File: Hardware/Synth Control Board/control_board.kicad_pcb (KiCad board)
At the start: 2 copper layers, 127 x 177.8 mm, 36 parts, among them J1 Conn_01x13, J2 Conn_01x03, J3 Conn_01x13, J4 Conn_01x13, J5 Conn_01x02, J6 Conn_01x13, SW1 SW_DPDT_x2, SW10 SW_SPST, SW11 SW_SPST, SW12 SW_SPST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

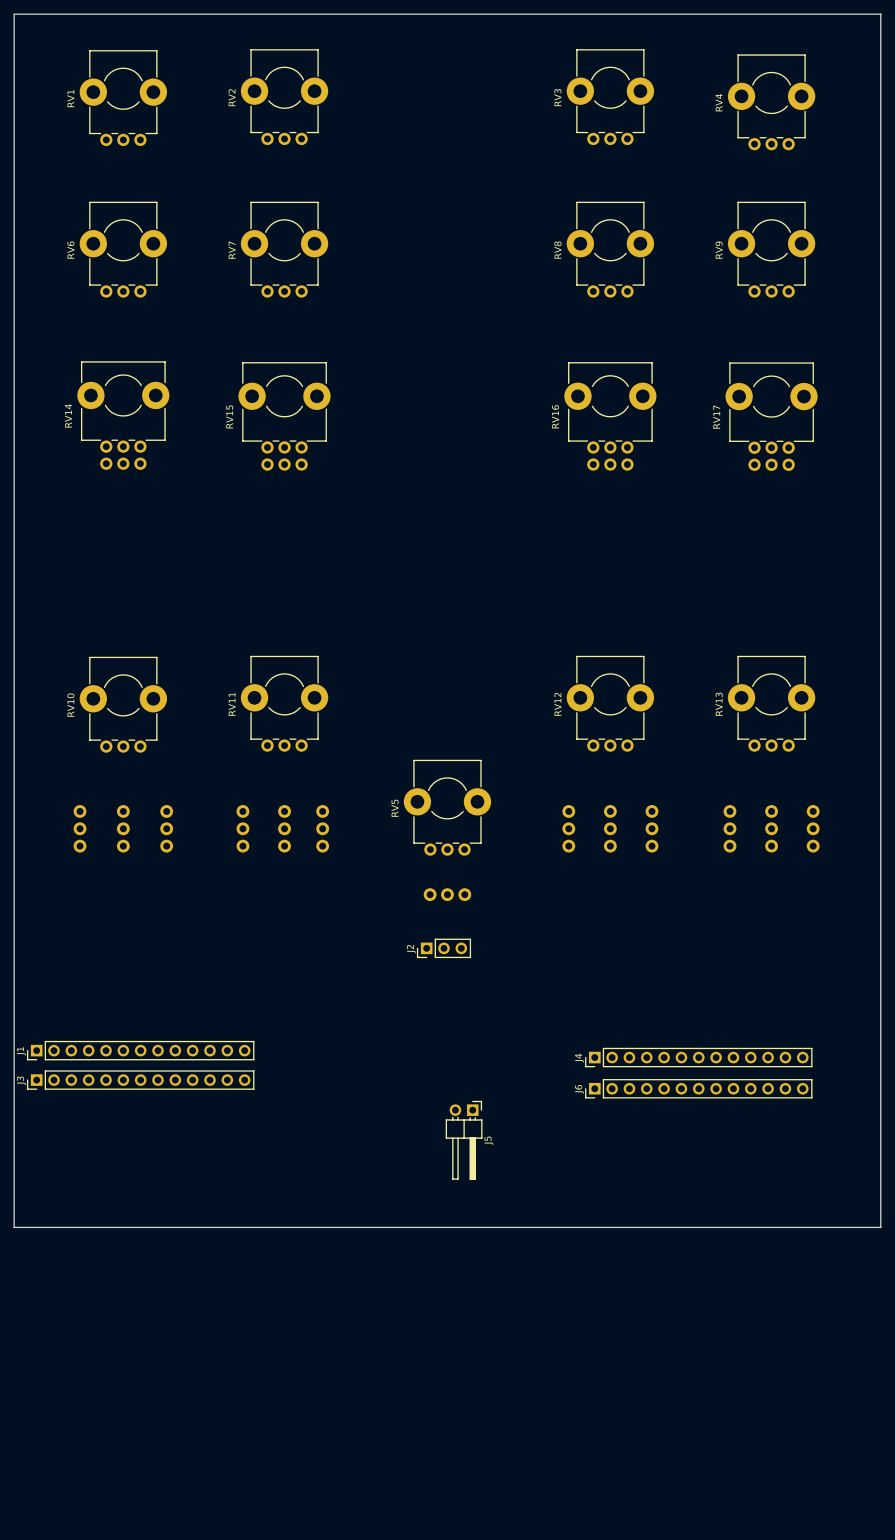
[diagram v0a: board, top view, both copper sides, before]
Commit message: add volume pots to control board
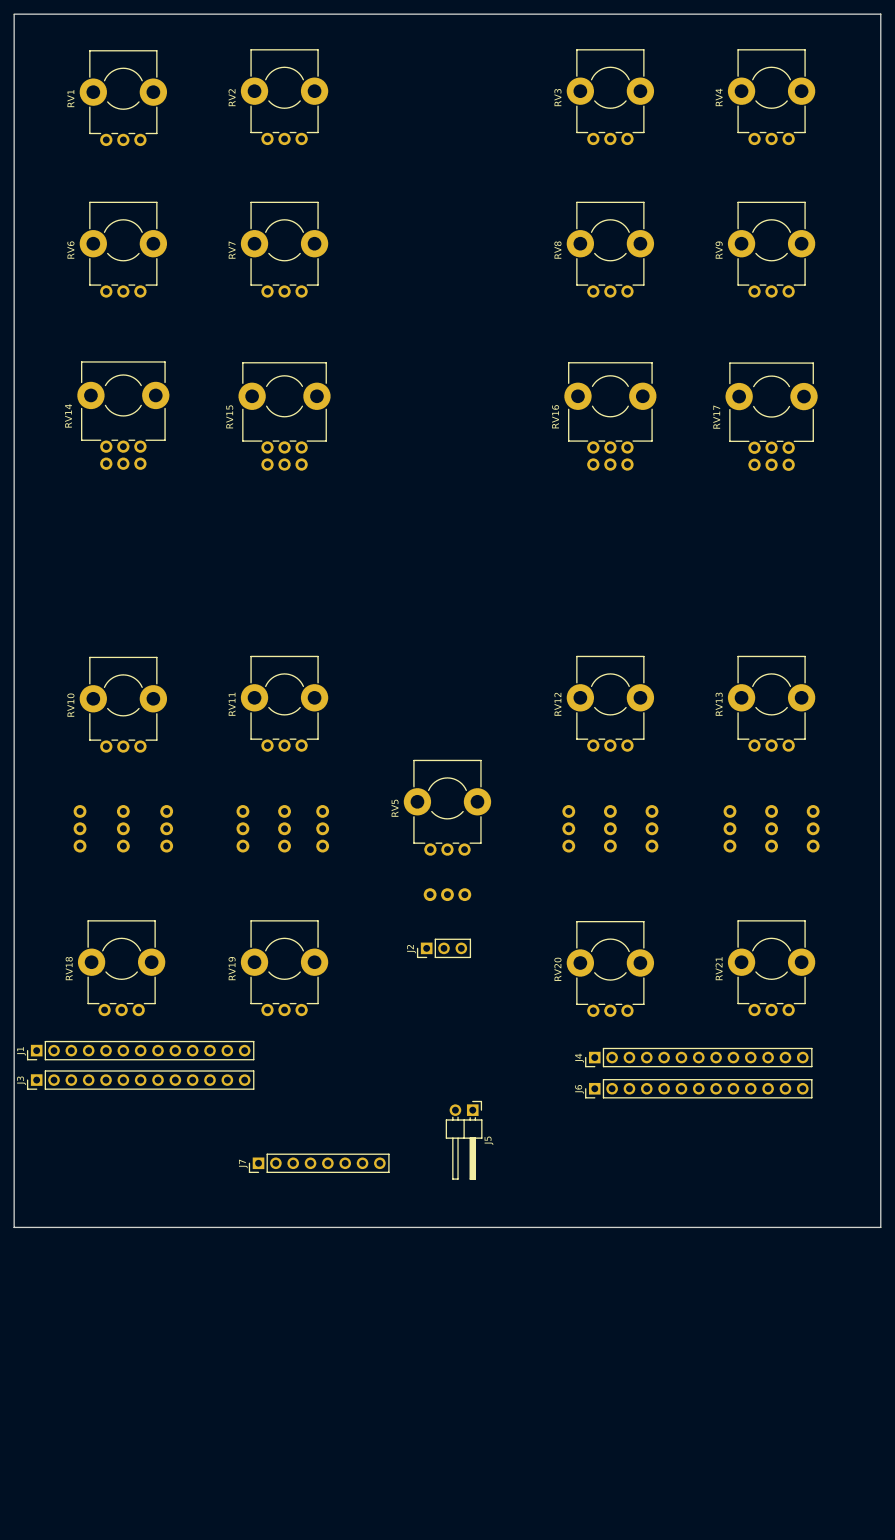
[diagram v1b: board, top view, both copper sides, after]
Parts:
- added J7: Conn_01x08, Pin_Headers:Pin_Header_Straight_1x08_Pitch2.54mm, F.Cu at (35.8, 168.4)
- added RV18: 100kA, Potentiometers:Potentiometer_Bourns_PTV09A-1_Horizontal, F.Cu at (18.2, 145.9)
- added RV19: 100kA, Potentiometers:Potentiometer_Bourns_PTV09A-1_Horizontal, F.Cu at (42.1, 145.9)
- added RV20: 100kA, Potentiometers:Potentiometer_Bourns_PTV09A-1_Horizontal, F.Cu at (89.9, 146.1)
- added RV21: 100kA, Potentiometers:Potentiometer_Bourns_PTV09A-1_Horizontal, F.Cu at (113.5, 145.9)
- moved RV4 0.76 mm to (113.5, 18.3)

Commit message: place MCU footprints
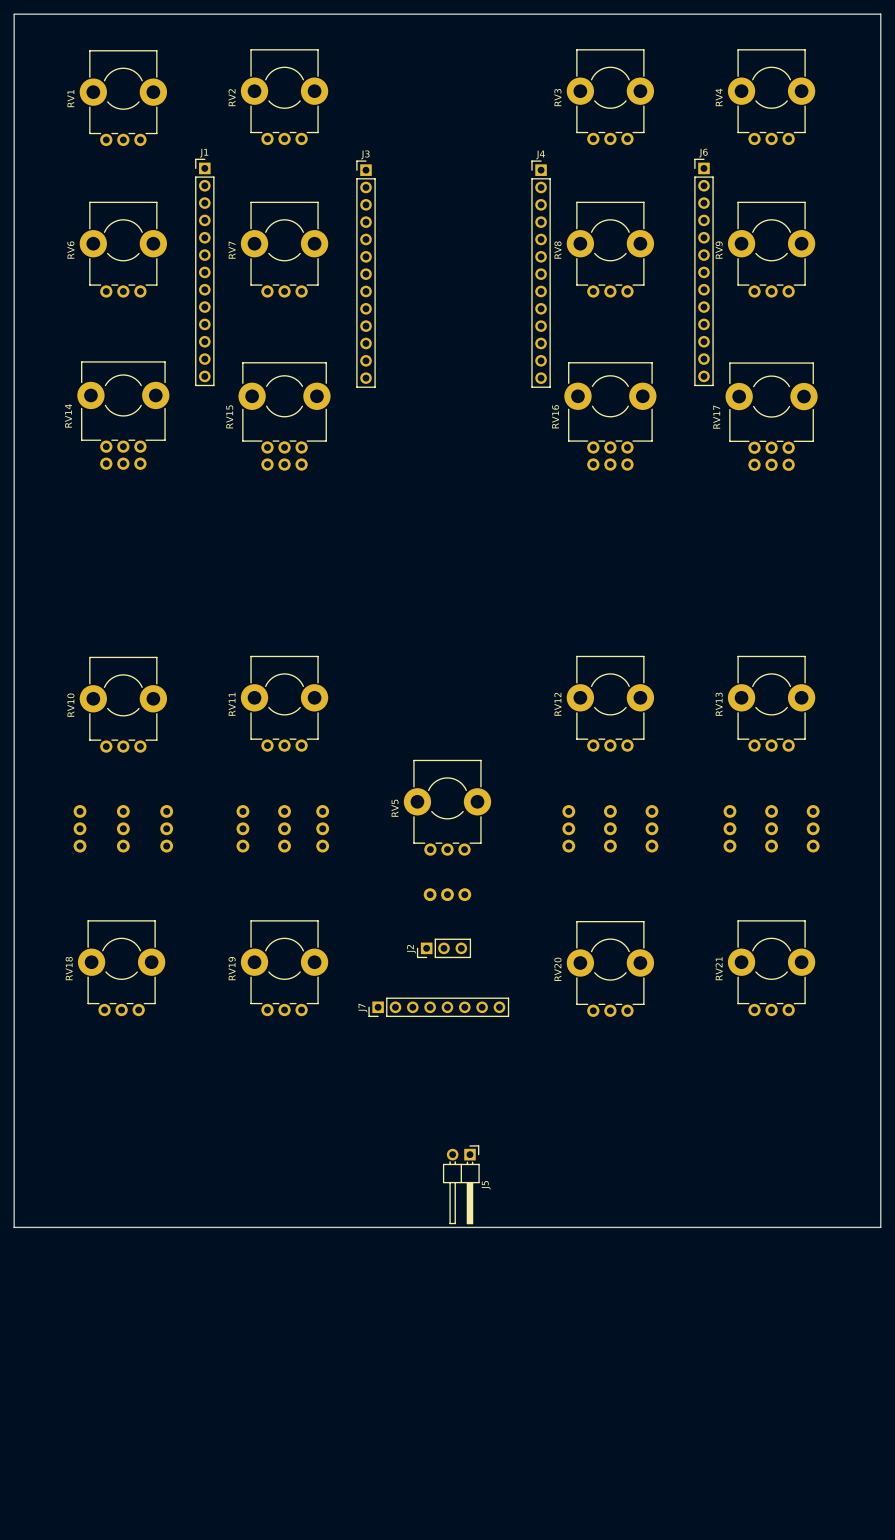
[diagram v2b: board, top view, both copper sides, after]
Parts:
- moved J3 141.8 mm to (51.6, 22.9), turned to 0 degrees
- moved J6 135.8 mm to (101.1, 22.6), turned to 0 degrees
- moved J1 131.6 mm to (27.9, 22.6), turned to 0 degrees
- moved J4 130.3 mm to (77.2, 22.9), turned to 0 degrees
- moved J7 28.8 mm to (53.3, 145.5)
- moved J5 6.53 mm to (66.8, 167.1)

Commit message: add LFO mod pots to control board and fix pot placement
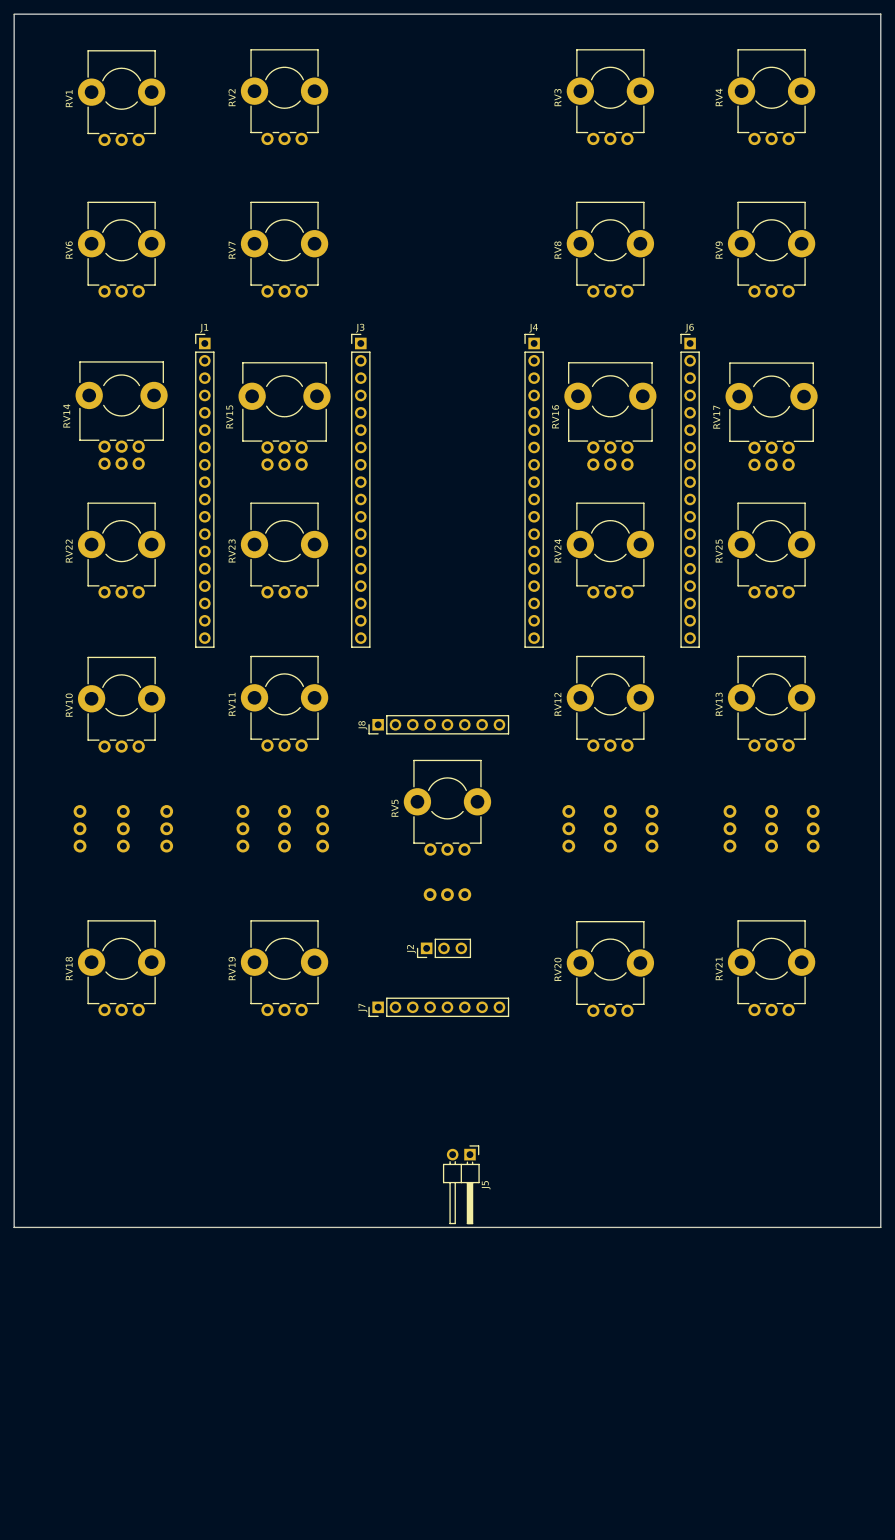
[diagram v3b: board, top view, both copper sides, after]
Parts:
- added J8: Conn_01x08, Pin_Headers:Pin_Header_Straight_1x08_Pitch2.54mm, F.Cu at (53.3, 104.1)
- added RV22: 100kA, Potentiometers:Potentiometer_Bourns_PTV09A-1_Horizontal, F.Cu at (18.2, 84.7)
- added RV23: 100kA, Potentiometers:Potentiometer_Bourns_PTV09A-1_Horizontal, F.Cu at (42.1, 84.7)
- added RV24: 100kA, Potentiometers:Potentiometer_Bourns_PTV09A-1_Horizontal, F.Cu at (89.9, 84.7)
- added RV25: 100kA, Potentiometers:Potentiometer_Bourns_PTV09A-1_Horizontal, F.Cu at (113.5, 84.7)
- J1, J3, J4, J6: value Conn_01x13 -> Conn_01x18; footprint Pin_Headers:Pin_Header_Straight_1x13_Pitch2.54mm -> Pin_Headers:Pin_Header_Straight_1x18_Pitch2.54mm
- moved J6 25.7 mm to (99.1, 48.3)
- moved J1 25.7 mm to (27.9, 48.3)
- moved J4 25.4 mm to (76.2, 48.3)
- moved J3 25.4 mm to (50.8, 48.3)
- moved RV1 0.25 mm to (18.2, 18.4)
- moved RV10 0.25 mm to (18.2, 107.3)
- moved RV14 0.25 mm to (18.2, 63.4)
- moved RV6 0.25 mm to (18.2, 40.6)
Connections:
- J1 pad 10: /osc1_repeat -> /osc1_speed
- J1 pad 11: /osc1_quant -> +5V
- J1 pad 12: GND -> /envelope_pwm_bypass_in_1
- J1 pad 13: GNDD -> /envelope_pwm_bypass_out_1
- J1 pad 4: /osc1_speed -> +5V
- J1 pad 5: /freq_in_1 -> /freq_out_1
- J1 pad 7: /freq_out_1 -> /freq_in_1
- J1 pad 8: /envelope_pwm_bypass_in_1 -> /lfo_in_1
- J1 pad 9: /envelope_pwm_bypass_out_1 -> /lfo_out_1
- J3 pad 10: /osc2_repeat -> /osc2_speed
- J3 pad 11: /osc2_quant -> +5V
- J3 pad 12: GND -> /envelope_pwm_bypass_in_2
- J3 pad 13: GNDD -> /envelope_pwm_bypass_out_2
- J3 pad 4: /osc2_speed -> +5V
- J3 pad 5: /freq_in_2 -> /freq_out_2
- J3 pad 7: /freq_out_2 -> /freq_in_2
- J3 pad 8: /envelope_pwm_bypass_in_2 -> /lfo_in_2
- J3 pad 9: /envelope_pwm_bypass_out_2 -> /lfo_out_2
- J4 pad 10: /osc3_repeat -> /osc3_speed
- J4 pad 11: /osc3_quant -> +5V
- J4 pad 12: GND -> /envelope_pwm_bypass_in_3
- J4 pad 13: GNDD -> /envelope_pwm_bypass_out_3
- J4 pad 4: /osc3_speed -> +5V
- J4 pad 5: /freq_in_3 -> /freq_out_3
- J4 pad 7: /freq_out_3 -> /freq_in_3
- J4 pad 8: /envelope_pwm_bypass_in_3 -> /lfo_in_3
- J4 pad 9: /envelope_pwm_bypass_out_3 -> /lfo_out_3
- J6 pad 10: /osc4_repeat -> /osc4_speed
- J6 pad 11: /osc4_quant -> +5V
- J6 pad 12: GND -> /envelope_pwm_bypass_in_4
- J6 pad 13: GNDD -> /envelope_pwm_bypass_out_4
- J6 pad 4: /osc4_speed -> +5V
- J6 pad 5: /freq_in_4 -> /freq_out_4
- J6 pad 7: /freq_out_4 -> /freq_in_4
- J6 pad 8: /envelope_pwm_bypass_in_4 -> /lfo_in_4
- J6 pad 9: /envelope_pwm_bypass_out_4 -> /lfo_out_4
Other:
- rule trace_min: 0.2 -> 0.0889

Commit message: route traces to bypass caps on MCU. control board and connectors are WIP.
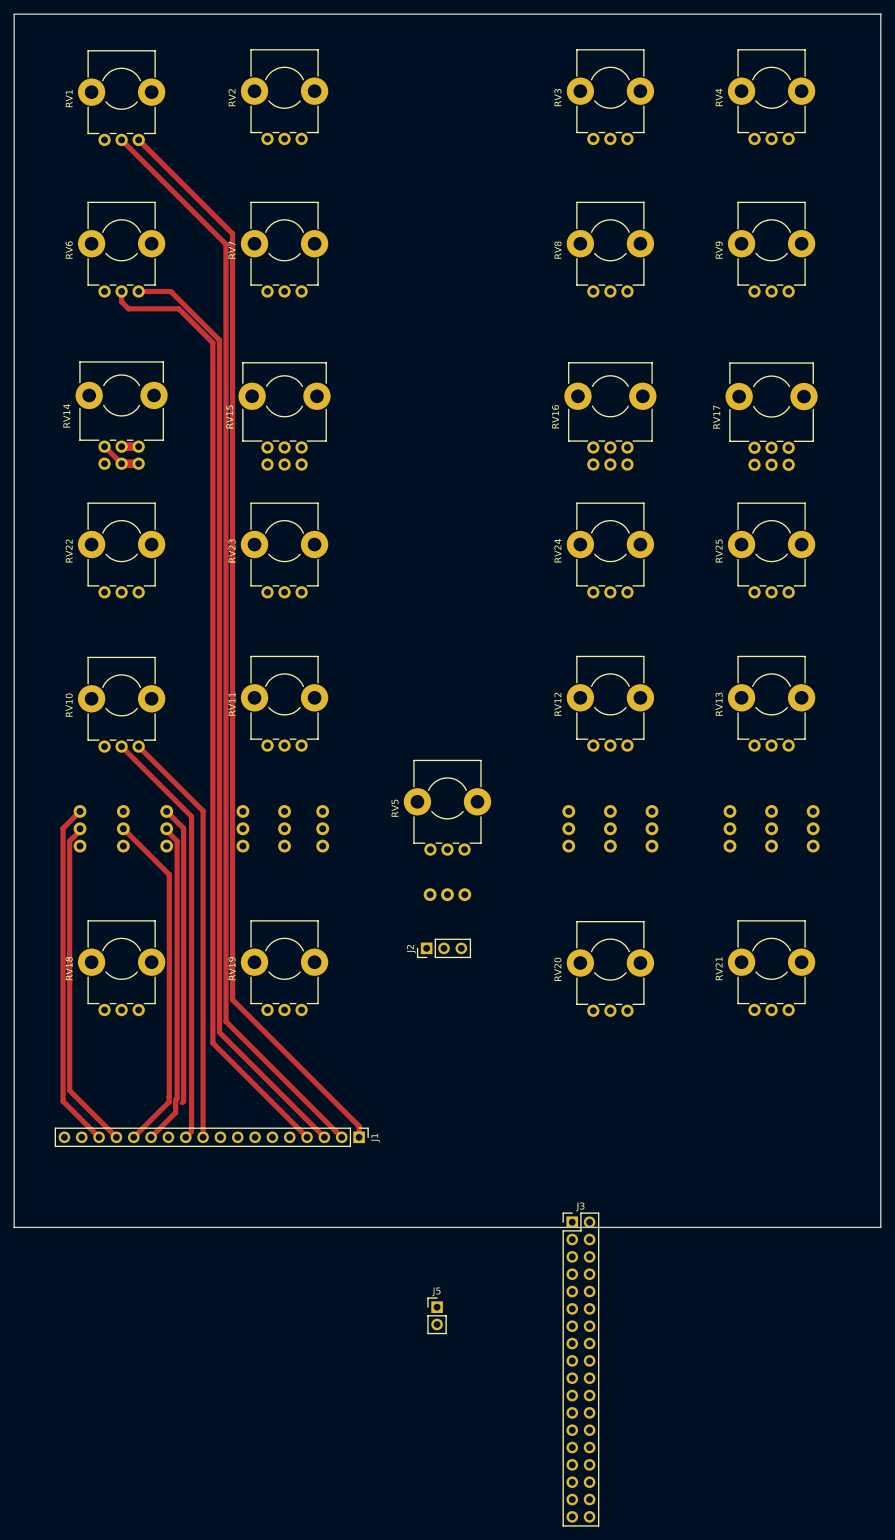
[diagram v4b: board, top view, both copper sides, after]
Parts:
- removed J4, J6: Conn_01x18, Pin_Headers:Pin_Header_Straight_1x18_Pitch2.54mm
- removed J7, J8: Conn_01x08, Pin_Headers:Pin_Header_Straight_1x08_Pitch2.54mm
- J3: value Conn_01x18 -> Conn_02x18_Odd_Even; footprint Pin_Headers:Pin_Header_Straight_1x18_Pitch2.54mm -> Pin_Headers:Pin_Header_Straight_2x18_Pitch2.54mm
- J5: footprint Pin_Headers:Pin_Header_Angled_1x02_Pitch2.54mm -> Pin_Headers:Pin_Header_Straight_1x02_Pitch2.54mm
- SW6, SW7: value SW_SPST -> SW_DPDT_x2
- moved J3 132.5 mm to (81.8, 177.0)
- moved J1 118.5 mm to (50.5, 164.6), turned to 270 degrees
- moved J5 22.9 mm to (62.0, 189.5), turned to 0 degrees
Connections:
- J1 pad 10: /osc1_speed -> +5V
- J1 pad 11: +5V -> /osc1_speed
- J1 pad 12: /envelope_pwm_bypass_in_1 -> /osc1_hold
- J1 pad 13: /envelope_pwm_bypass_out_1 -> /osc1_repeat
- J1 pad 15: /osc1_hold -> /envelope_pwm_bypass_out_1
- J1 pad 16: /osc1_repeat -> /envelope_pwm_bypass_in_1
- J1 pad 3: /osc1_pwm_wiper -> +5V
- J1 pad 4: +5V -> /osc1_pwm_wiper
- J1 pad 5: /freq_out_1 -> /freq_in_1
- J1 pad 7: /freq_in_1 -> /freq_out_1
- J3 pad 10: /osc2_speed -> /freq_out_4
- J3 pad 11: +5V -> /freq_fb_3
- J3 pad 12: /envelope_pwm_bypass_in_2 -> /freq_fb_4
- J3 pad 13: /envelope_pwm_bypass_out_2 -> /freq_in_3
- J3 pad 14: /osc2_quant -> /freq_in_4
- J3 pad 15: /osc2_hold -> /lfo_out_3
- J3 pad 16: /osc2_repeat -> /lfo_in_4
- J3 pad 17: GND -> /lfo_in_3
- J3 pad 18: GNDD -> /lfo_out_4
- J3 pad 2: /osc2_freq_wiper -> +5V
- J3 pad 3: /osc2_pwm_wiper -> /osc3_freq_wiper
- J3 pad 4: +5V -> /osc4_freq_wiper
- J3 pad 5: /freq_out_2 -> /osc3_pwm_wiper
- J3 pad 6: /freq_fb_2 -> /osc4_pwm_wiper
- J3 pad 7: /freq_in_2 -> +5V
- J3 pad 8: /lfo_in_2 -> +5V
- J3 pad 9: /lfo_out_2 -> /freq_out_3
- RV18 pad 1: Net-(J7-Pad1) -> /vol_in_1
- RV18 pad 2: Net-(J7-Pad2) -> /vol_out_1
- RV19 pad 1: Net-(J7-Pad3) -> /vol_in_2
- RV19 pad 2: Net-(J7-Pad4) -> /vol_out_2
- RV20 pad 1: Net-(J7-Pad5) -> /vol_in_3
- RV20 pad 2: Net-(J7-Pad6) -> /vol_out_3
- RV21 pad 1: Net-(J7-Pad7) -> /vol_in_4
- RV21 pad 2: Net-(J7-Pad8) -> /vol_out_4
- RV22 pad 1: Net-(J8-Pad1) -> /lfo_in_1
- RV22 pad 2: Net-(J8-Pad2) -> /lfo_out_1
- RV23 pad 1: Net-(J8-Pad3) -> /lfo_in_2
- RV23 pad 2: Net-(J8-Pad4) -> /lfo_out_2
- RV24 pad 1: Net-(J8-Pad5) -> /lfo_in_3
- RV24 pad 2: Net-(J8-Pad6) -> /lfo_out_3
- RV25 pad 1: Net-(J8-Pad7) -> /lfo_in_4
- RV25 pad 2: Net-(J8-Pad8) -> /lfo_out_4
- SW6 pad 1: GNDD -> /osc1_repeat
- SW6 pad 2: /osc4_repeat -> GNDD
- SW6 pad 3: (no net) -> /osc1_hold
- SW7 pad 1: GNDD -> /osc3_repeat
- SW7 pad 2: /osc3_repeat -> GNDD
- SW7 pad 3: (no net) -> /osc3_hold
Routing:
- net +5V: track 0.00 -> 358.7 mm
- net /osc1_freq_wiper: track 0.00 -> 159.5 mm
- net /osc1_pwm_wiper: track 0.00 -> 139.5 mm
- net /osc1_speed: track 0.00 -> 61.9 mm
- net /envelope_pwm_bypass_in_1: track 0.00 -> 51.0 mm
- net /osc1_quant: track 0.00 -> 50.2 mm
- net /envelope_pwm_bypass_out_1: track 0.00 -> 48.7 mm
- net /osc1_repeat: track 0.00 -> 47.4 mm
- net GNDD: track 0.00 -> 43.8 mm
- net /freq_fb_1: track 0.00 -> 6.04 mm
- net /freq_in_1: track 0.00 -> 2.50 mm
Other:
- rule via_min_drill: 0.3 -> 0.2
- rule via_min_size: 0.4 -> 0.45
